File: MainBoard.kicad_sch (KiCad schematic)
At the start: 83 parts, among them J1 Conn_01x04, J10 Conn_01x08, J11 Conn_01x03, J12 Conn_01x04, J13 Conn_01x03, J14 Conn_01x03, J15 Conn_01x05, J16 Conn_01x04, J17 Conn_01x03, J18 Conn_01x03, J19 Conn_01x05, J2 Conn_01x04, J20 Conn_01x05, J21 Conn_01x04, J22 Conn_01x04, J23 Conn_01x04, J24 Conn_01x04, J25 Conn_01x04, J26 Conn_01x05, J27 Conn_01x06, J3 Conn_01x04, J4 Conn_01x04, J5 Conn_01x06, J6 Conn_01x02, J7 Conn_01x02, J8 Conn_01x02, J9 Conn_01x02, Q1 NMOS, Q10 NMOS, Q11 NMOS, Q2 NMOS, Q3 NMOS, Q4 NMOS, Q5 NMOS, Q6 NMOS, Q7 NMOS, Q8 NMOS, Q9 NMOS, U1 INA228, U2 INA228, U4 MCP23017_SO, U5 MCP23017_SO, U6 ESP32-DEVKITC-32D, U7 TJA1051T, U8 INA228, U9 INA228

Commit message: reorganized sheeet
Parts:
- removed D10, D13, D14, D9: WS2812B, LED_SMD:LED_WS2812B_PLCC4_5.0x5.0mm_P3.2mm, symbol LED:WS2812B
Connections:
- net GND: now also D8.3 (VSS)
- no-connect marks 5 -> 6
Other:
- note added: "0.3 CHF N-Channel Power MOSFET, 100 V, 10 A, 180 mΩ"
- note added: "2A MAX"
- note added: "2A max"
- note added: "Blinker + Trunk Latch + Int light"
- note added: "Compute"
- note added: "LOGICLEVELSHIFTER !"
- note added: "Latch Trunk Interrior Lightning"
- note added: "Seat + Hand Warmer Brake + seat sensor"
- note removed: "5A MAX (more likely 1A max)"
- note removed: "Blinker + Seat & Hand Warmer Brake + seat sensor"
- note removed: "Latch Trunk Interrior Lightnint"
- moved on the sheet: C1, C3, C4, C5, D1, D11, D12, D2, D3, D4, D5, D6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

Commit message: schematic done, only INA228 left to size
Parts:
- removed F1, F2, F3: Fuse, symbol Device:Fuse
- removed Q2: NMOS, symbol Simulation_SPICE:NMOS
- removed U7: TJA1051T, Package_SO:SOIC-8_3.9x4.9mm_P1.27mm, symbol Interface_CAN_LIN:TJA1051T
- added C1: 100nF, symbol Device:C
- added D4: US1M, Diode_SMD:D_SMA, symbol Diode:US1M
- added Q3: NMOS, symbol Simulation_SPICE:NMOS
- added R3, R4, R5: 100R, symbol Device:R
- added U1: TJA1051T-3, Package_SO:SOIC-8_3.9x4.9mm_P1.27mm, symbol Interface_CAN_LIN:TJA1051T-3
- added U4: ~, symbol velion_mainboard:buck12V
- R6: renamed from R3; value R -> 4k7
- R7: renamed from R4; value R -> 4k7
- renumbered C3 to C2, C2 to C3, C1 to C4, C4 to C5, C5 to C6, D7 to D10, D8 to D11, D3 to D2, D2 to D3, D4 to D5, D5 to D6, D6 to D7, D11 to D8, D12 to D9, F4 to F1, J13 to J10, J14 to J11, J11 to J13, J16 to J14, J26 to J16, J27 to J17, J19 to J18, J10 to J19, J18 to J20, J17 to J21, J20 to J22, J21 to J23, J22 to J24, J23 to J25, J24 to J26, J25 to J27, J5 to J3, J6 to J4, J7 to J5, J3 to J6, J4 to J7, J9 to J8, J8 to J9, Q3 to Q2, R2 to R1, R5 to R10, R6 to R11, R9 to R12, R10 to R13, R11 to R14, R12 to R15, R13 to R16, R1 to R2, R7 to R8, R8 to R9, U9 to U10, U1 to U5, U5 to U7, U4 to U8, U8 to U9
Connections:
- net +3.3V: now also J19.2 (Pin_2), R6.1, R7.1, U7.15 (A0), U7.18 (~{RESET}), U8.18 (~{RESET}), C1.1, U1.5 (VIO); no longer C2.1, U10.1 (A1), U9.2 (A0)
- net +5V: now also C2.1, U3.2 (5VOUT), D4.2 (A), U1.3 (VCC); no longer D5.1 (VDD), J19.1 (Pin_1), U3. (GND)
- net AUXAUDIO_MOSFET_GATE: now also U7.21 (GPA0)
- net AUXUSB_MOSFET_GATE: now also U7.22 (GPA1), Q3.2 (G)
- net BLINKER_LEFT_MOSFET_GATE: now also Q4.2 (G), R4.1; no longer Q5.2 (G)
- net BLINKER_RIGHT_MOSFET_GATE: now also R5.1
- net BRAKE_LEFT_INPUT: now also U8.22 (GPA1)
- net BRAKE_RIGHT_INPUT: now also U8.21 (GPA0)
- net BROUILLARD_INPUT: now also U8.25 (GPA4)
- net BROUILLARD_LED: now also U7.5 (GPB4)
- net CABLIGHT_INPUT: now also U8.26 (GPA5)
- net CABLIGHT_LED: now also U7.2 (GPB1)
- net CANH: now also J3.6 (Pin_6), U1.7 (CANH); no longer J3.4 (Pin_4)
- net CANL: now also J3.5 (Pin_5), U1.6 (CANL); no longer J3.3 (Pin_3)
- net CAN_RX: now also U6.J3-8 (IO19), U1.4 (RXD)
- net CAN_S: now also U6.J2-13 (IO12), U1.8 (S)
- net CAN_TX: now also U6.J3-9 (IO18), U1.1 (TXD)
- net DEFROSTER_MOSFET_GATE: now also U6.J2-15 (IO13)
- net DEFROST_INPUT: now also U7.7 (GPB6)
- net DEFROST_LED: now also U7.3 (GPB2)
- net DRL_LEFT_MOSFET_GATE: now also Q5.2 (G), U6.J3-11 (IO17); no longer Q8.2 (G)
- net DRL_RIGHT_MOSFET_GATE: now also Q7.2 (G), U6.J3-12 (IO16); no longer Q9.2 (G)
- net Defroster_ALERT: now also U8.1 (GPB0)
- net FORWARD_INPUT: now also U8.24 (GPA3)
- net GND: now also J3.2 (Pin_2), U10.1 (A1), U3.3 (GND), U3.4 (GND), U7.16 (A1), U7.17 (A2), U8.15 (A0), U8.16 (A1), U8.17 (A2), U9.2 (A0), C1.2, Q3.3 (S), U1.2 (GND), U4.3 (GND), U4.4 (GND); no longer U3. (GND)
- net HANDHEATER_ALERT: now also U8.2 (GPB1)
- net HANDHEATER_MOSFET_GATE: now also U6.J3-13 (IO4)
- net INTERRIOR_LIGHT_MOSFET_GATE: now also Q8.2 (G), R3.1; no longer Q4.2 (G)
- net LATCH_TRUNK_MOSFET_GATE: now also Q9.2 (G), U7.23 (GPA2); no longer Q7.2 (G)
- net MAP_INPUT: now also U8.28 (GPA7)
- net MAP_LED: now also U7.6 (GPB5)
- net PAS_A: now also U6.J2-11 (IO27)
- net PAS_B: now also U6.J2-12 (IO14)
- net POT_HANDHEATER_A: now also U6.J2-9 (IO25)
- net POT_HANDHEATER_B: now also U6.J2-10 (IO26)
- net POT_HANDHEATER_X: now also U8.5 (GPB4)
- net POT_SEATDHEATER_X: now also U8.6 (GPB5)
- net POT_SEATHEATER_A: now also U6.J2-7 (IO32)
- net POT_SEATHEATER_B: now also U6.J2-8 (IO33)
- net POT_SPEED_A: now also U6.J2-5 (IO34)
- net POT_SPEED_B: now also U6.J2-6 (IO35)
- net POT_SPEED_X: now also U8.7 (GPB6)
- net POWERINPUT_ALERT: now also U8.4 (GPB3)
- net REVERSE_INPUT: now also U8.23 (GPA2)
- net RGBLED_DIN: now also D5.4 (DIN), U6.J3-6 (IO21)
- net SCL: now also R7.2, U6.J3-3 (IO22), U7.12 (SCK), U8.12 (SCK)
- net SDA: now also R6.2, U6.J3-2 (IO23), U7.13 (SDA), U8.13 (SDA)
- net SEATHEATER_ALERT: now also U8.3 (GPB2)
- net SEATHEATER_MOSFET_GATE: now also U6.J3-10 (IO5)
- net SEAT_INPUT: now also U8.8 (GPB7)
- net THROTTLE_INPUT: now also U6.J2-3 (SENSOR_VP)
- net TRUNK_INPUT: now also U7.8 (GPB7)
- net TRUNK_LED: now also U7.4 (GPB3)
- net VBUS: now also U3.1 (VIN), U4.1 (VIN); no longer J10.1 (Pin_1), J11.1 (Pin_1), J12.1 (Pin_1), J12.3 (Pin_3), U3. (GND)
- net WARNING_INPUT: now also U8.27 (GPA6)
- net WARNING_LED: now also U7.1 (GPB0)
- net at J10.2 (Pin_2): now also Q4.1 (D); no longer Q5.1 (D)
- net at J10.3 (Pin_3): now also Q5.1 (D); no longer Q8.1 (D)
- net at J11.3 (Pin_3): now also Q7.1 (D); no longer Q9.1 (D)
- net at J12.4 (Pin_4): now also Q9.1 (D); no longer Q7.1 (D)
- net at J12.2 (Pin_2): now also Q8.1 (D); no longer Q4.1 (D)
- net at J4.2 (Pin_2), R1.1, U2.10 (Vin+)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: now also J3.3 (Pin_3), J3.4 (Pin_4); no longer J3.2 (Pin_2)
- net at D3.2 (A), J9.1 (Pin_1): now also Q3.1 (D)
- net InterruptEXTGPIO: now reaches U8.20 (INTA)
- net InterruptEXTGPIO: now also U6.J2-4 (SENSOR_VN)
- net at U6.J3-14 (IO0): now also R5.2
- net at U6.J3-15 (IO2): now also R4.2
- net at U6.J3-16 (IO15): now also R3.2
- new net: D4.1 (K), D5.1 (VDD)
- new net +12V: J10.1 (Pin_1), J11.1 (Pin_1), J12.1 (Pin_1), J12.3 (Pin_3), U4.2 (5VOUT)
- no-connect marks 6 -> 23
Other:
- note added: "+ + - -"
- note added: "0100000 = 0x20"
- note added: "0100001 = 0x21"
- note added: "1000000 -> 0x40"
- note added: "1000001 -> 0x41"
- note added: "1000100 -> 0x44"
- note added: "1000101 -> 0x45"
- note added: "10A Fuse here"
- note added: "35-60V"
- note added: "3v3 provided by internal LDO of ESP32 devboard"
- note added: "40A Fuse Here"
- note added: "40A Fuse here"
- note added: "MPU9250 : 1101000 -> 0x68 BMP280 : 1110110 -> 0x76"
- note added: "diode -> little hack to drive the WS2812 using 3v3 logic"
- note added: "https://hackaday.com/2017/01/20/cheating-at-5v-ws2812-control-to-use-a-3-3v-data-line/"
- note added: "leave serial port for debug"
- note added: "resistor to limit risk of issue due to current leakage and the mosfet grid capacitor that could influence the strapping pin at boot."
- note added: "small sig 20 V 5A mosfet"
- note removed: "0.3 CHF N-Channel Power MOSFET, 100 V, 10 A, 180 mΩ"
- note removed: "0.3 CHF N-Channel Power MOSFET, Logic Level, QFET®, 100 V, 10 A, 180 mΩ"
- note removed: "40A"
- note removed: "LOGICLEVELSHIFTER !"
- note removed: "should in theory also work with 3V3 but if LDO is cheap, we have issue..."
- note removed: "~47 IO, need to shrink"
- moved on the sheet: C2, C3, C4, D10, D11, D2, D5, D6, D7, F1, J13, J14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

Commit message: BOM done, pcb layout done, routing ...
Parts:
- removed F1: Fuse, symbol Device:Fuse
- removed Q1, Q10, Q11, Q2, Q3, Q4, Q5, Q6, Q7, Q8, Q9: NMOS, symbol Simulation_SPICE:NMOS
- added J6: Conn_01x02, velion_mainboard:15EDG-2P, symbol Connector_Generic:Conn_01x02
- added Q1, Q10, Q11, Q2, Q3: NMOS_80A, velion_mainboard:NMOS_80A, symbol Transistor_FET_Other:Q_NMOS_Depletion_GDS
- added Q4, Q5, Q6, Q7, Q8, Q9: NMOS, Package_TO_SOT_SMD:SOT-23, symbol Transistor_FET_Other:Q_NMOS_Depletion_GSD
- C1, C2, C3, C4, C5, C6: footprint (none) -> Capacitor_SMD:C_1206_3216Metric_Pad1.33x1.80mm_HandSolder
- J1, J2: footprint (none) -> velion_mainboard:15EDG-4P
- J10: renamed from J9; footprint (none) -> velion_mainboard:15EDG-2P
- J11: renamed from J10; footprint (none) -> velion_mainboard:15EDG-3P
- J12: renamed from J11; footprint (none) -> velion_mainboard:15EDG-3P
- J13: renamed from J12; footprint (none) -> velion_mainboard:15EDG-4P
- J14: renamed from J13; footprint (none) -> velion_mainboard:15EDG-3P
- J15: renamed from J14; footprint (none) -> velion_mainboard:15EDG-4P
- J16: renamed from J15; footprint (none) -> velion_mainboard:15EDG-5P
- J17: renamed from J16; footprint (none) -> velion_mainboard:15EDG-5P
- J18: renamed from J17; footprint (none) -> velion_mainboard:15EDG-6P
- J19: renamed from J18; footprint (none) -> velion_mainboard:15EDG-5P
- J20: renamed from J19; footprint (none) -> velion_mainboard:GY-91
- J21: renamed from J20; footprint (none) -> velion_mainboard:15EDG-3P
- J22: renamed from J21; footprint (none) -> velion_mainboard:15EDG-3P
- J23: renamed from J22; footprint (none) -> velion_mainboard:15EDG-5P
- J24: renamed from J23; footprint (none) -> velion_mainboard:15EDG-4P
- J25: renamed from J24; footprint (none) -> velion_mainboard:15EDG-4P
- J26: renamed from J25; footprint (none) -> velion_mainboard:15EDG-4P
- J27: renamed from J26; footprint (none) -> velion_mainboard:15EDG-4P
- J28: renamed from J27; footprint (none) -> velion_mainboard:15EDG-4P
- J3: footprint (none) -> velion_mainboard:15EDG-6P
- J4, J5: footprint (none) -> velion_mainboard:15EDG-2P
- J7: renamed from J6; footprint (none) -> velion_mainboard:15EDG-4P
- J8: renamed from J7; footprint (none) -> velion_mainboard:15EDG-4P
- J9: renamed from J8; footprint (none) -> velion_mainboard:15EDG-2P
- R1, R2, R8, R9: value R -> 0.001 R; footprint (none) -> Resistor_SMD:R_2512_6332Metric_Pad1.40x3.35mm_HandSolder
- R10, R12, R13, R14, R15, R16: value 330 R -> 100 R; footprint (none) -> Resistor_SMD:R_1206_3216Metric_Pad1.30x1.75mm_HandSolder
- R11, R3, R4, R5, R6, R7: footprint (none) -> Resistor_SMD:R_1206_3216Metric_Pad1.30x1.75mm_HandSolder
- U3: footprint (none) -> velion_mainboard:BUCK5V
- U4: footprint (none) -> velion_mainboard:BUCK12V
- U6: footprint ESP32-DEVKITC-32D:MODULE_ESP32-DEVKITC-32D -> velion_mainboard:MODULE_ESP32-DEVKITC-32D
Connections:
- net AUXAUDIO_MOSFET_GATE: now also Q1.1 (G)
- net AUXUSB_MOSFET_GATE: now also Q3.1 (G)
- net BLINKER_LEFT_MOSFET_GATE: now also Q4.1 (G)
- net BLINKER_RIGHT_MOSFET_GATE: now also Q6.1 (G)
- net DEFROSTER_MOSFET_GATE: now also Q2.1 (G)
- net DRL_LEFT_MOSFET_GATE: now also Q5.1 (G)
- net DRL_RIGHT_MOSFET_GATE: now also Q7.1 (G)
- net GND: now also Q1.3 (S), Q10.3 (S), Q11.3 (S), Q2.3 (S), Q3.3 (S), Q4.2 (S), Q5.2 (S), Q6.2 (S), Q7.2 (S), Q8.2 (S), Q9.2 (S)
- net HANDHEATER_MOSFET_GATE: now also Q11.1 (G)
- net INTERRIOR_LIGHT_MOSFET_GATE: now also Q8.1 (G)
- net LATCH_TRUNK_MOSFET_GATE: now also Q9.1 (G)
- net SEATHEATER_MOSFET_GATE: now also Q10.1 (G)
- net VBUS: now also J6.2 (Pin_2)
- net VBUS_CAN_FUSED: now also J6.1 (Pin_1)
- net at J11.2 (Pin_2): now also Q4.3 (D)
- net at J11.3 (Pin_3): now also Q5.3 (D)
- net at D2.2 (A), J9.1 (Pin_1): now also Q2.2 (D)
- net at D9.2 (A), J18.2 (Pin_2): now also Q11.2 (D)
- net at D1.2 (A), J5.1 (Pin_1): now also Q1.2 (D)
- net at D8.2 (A), J17.2 (Pin_2): now also Q10.2 (D)
- net at J12.2 (Pin_2): now also Q6.3 (D)
- net at J12.3 (Pin_3): now also Q7.3 (D)
- net at J13.2 (Pin_2): now also Q8.3 (D)
- net at J13.4 (Pin_4): now also Q9.3 (D)
- net at D3.2 (A), J10.1 (Pin_1): now also Q3.2 (D)
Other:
- note added: "(3V3-2V)/10 mA=100 R"
- note added: "Fuse"
- note removed: "(5V-2V)/10 mA=330 R"

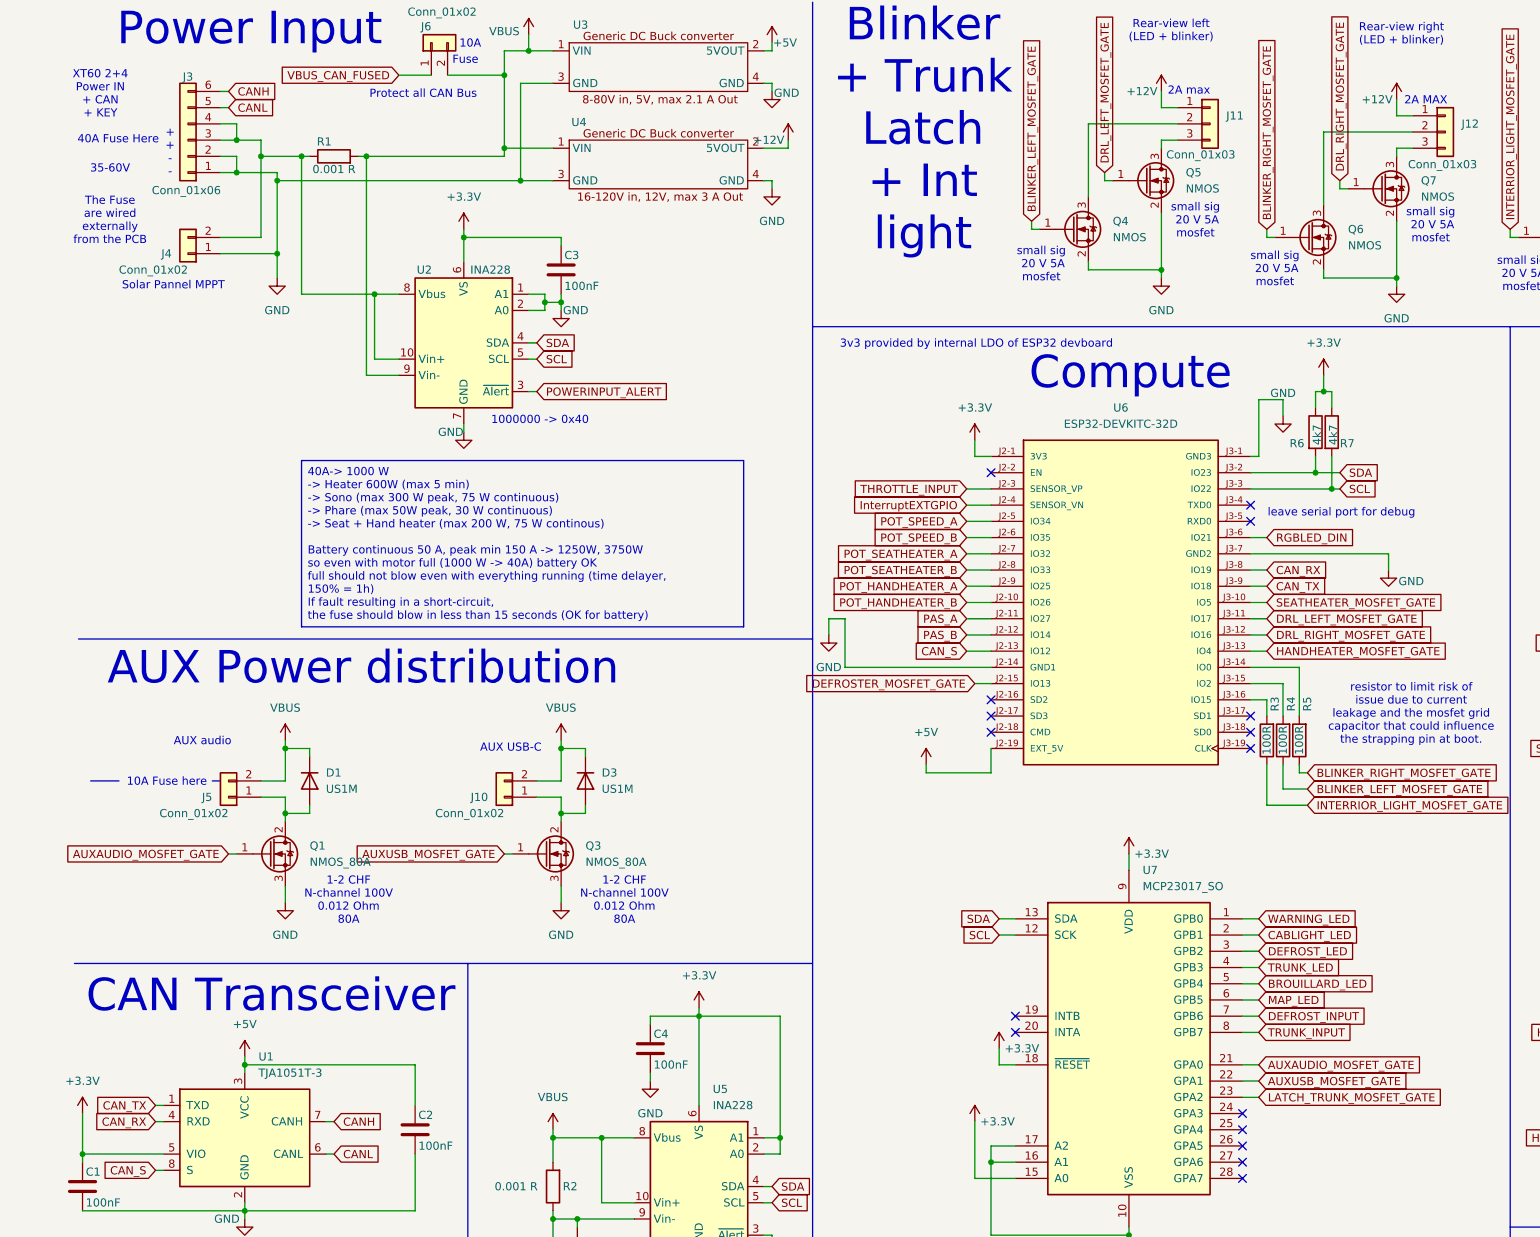
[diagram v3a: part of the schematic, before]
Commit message: added POWER signal for siliXcon
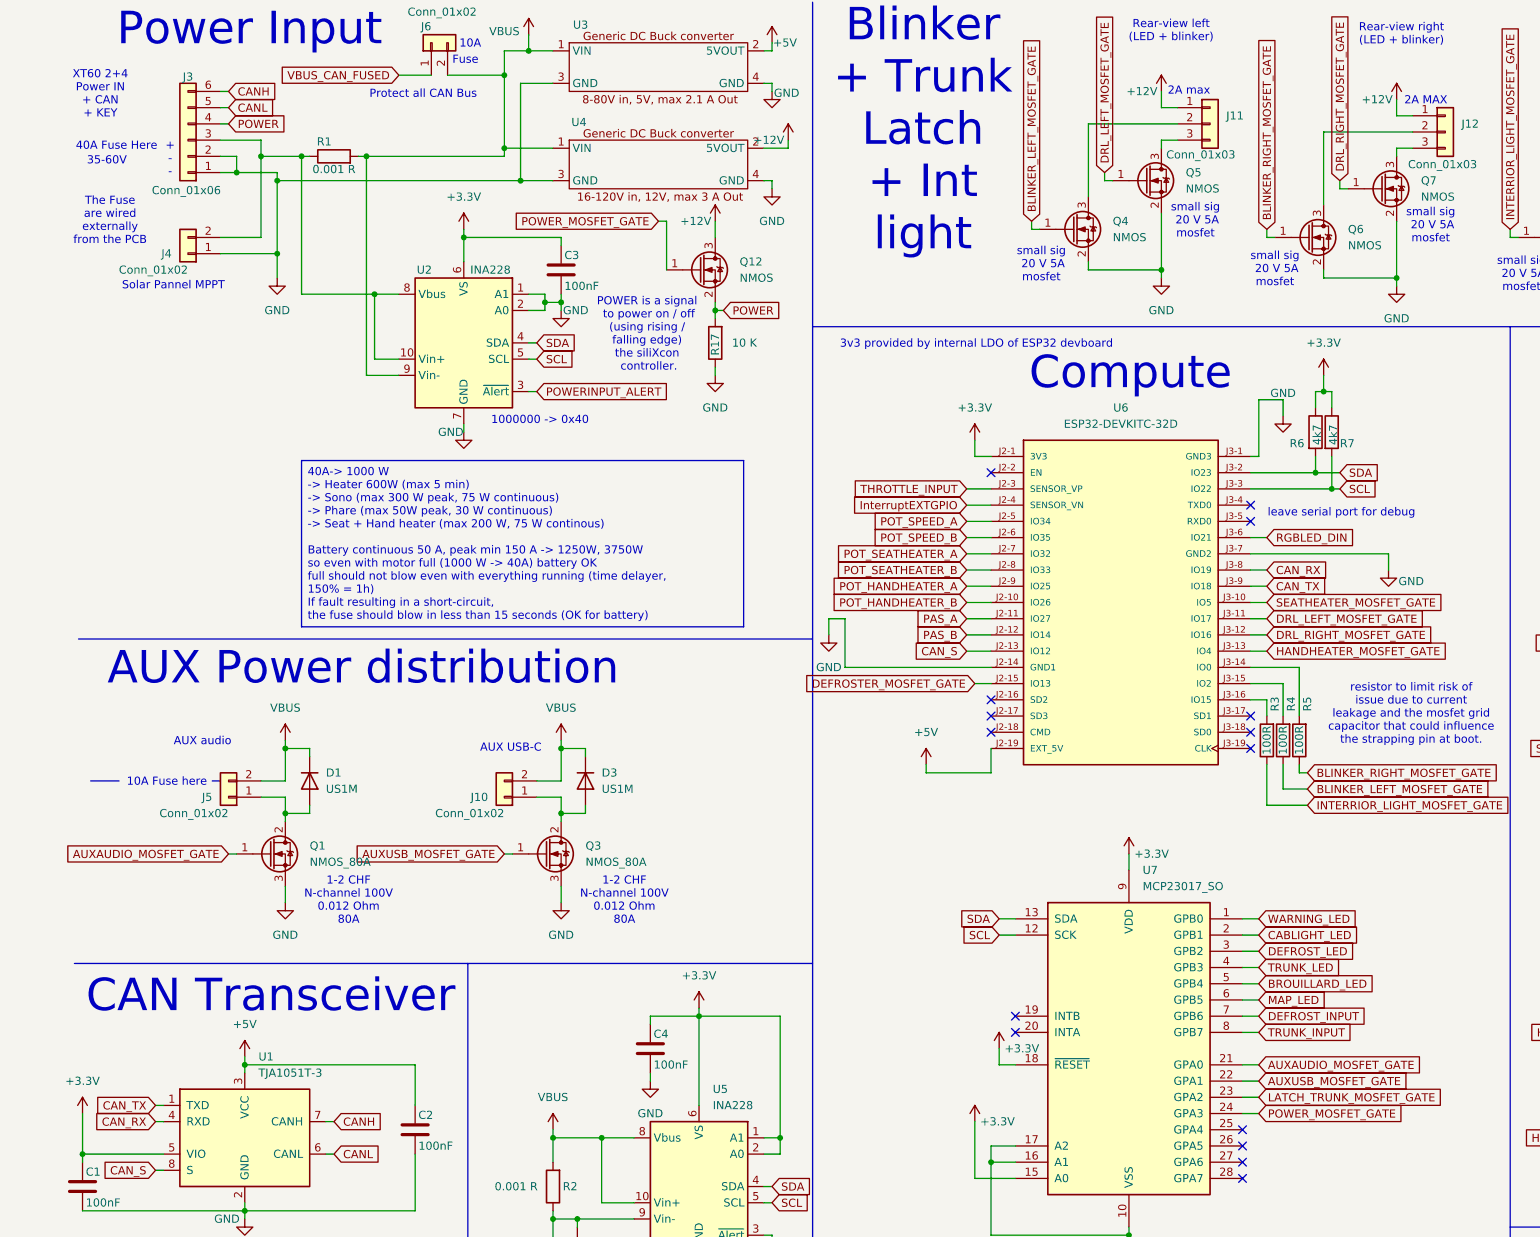
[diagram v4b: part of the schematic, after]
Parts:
- added Q12: NMOS, Package_TO_SOT_SMD:SOT-23, symbol Transistor_FET_Other:Q_NMOS_Depletion_GSD
- added R17: 10 K, Resistor_SMD:R_1206_3216Metric_Pad1.30x1.75mm_HandSolder, symbol Device:R
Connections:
- net +12V: now also Q12.3 (D)
- net GND: now also R17.1
- net at J3.3 (Pin_3), J4.2 (Pin_2), R1.1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: no longer J3.4 (Pin_4)
- net POWER_MOSFET_GATE: now reaches U7.24 (GPA3)
- net POWER_MOSFET_GATE: now also Q12.1 (G)
- new net POWER: J3.4 (Pin_4), Q12.2 (S), R17.2
- no-connect marks 23 -> 22
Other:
- note added: "+ - -"
- note added: "POWER is a signal to power on / off (using rising / falling edge) the siliXcon controller."
- note removed: "+ + - -"
